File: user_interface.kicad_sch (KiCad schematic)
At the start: 14 parts, among them SW901 SW_SPDT

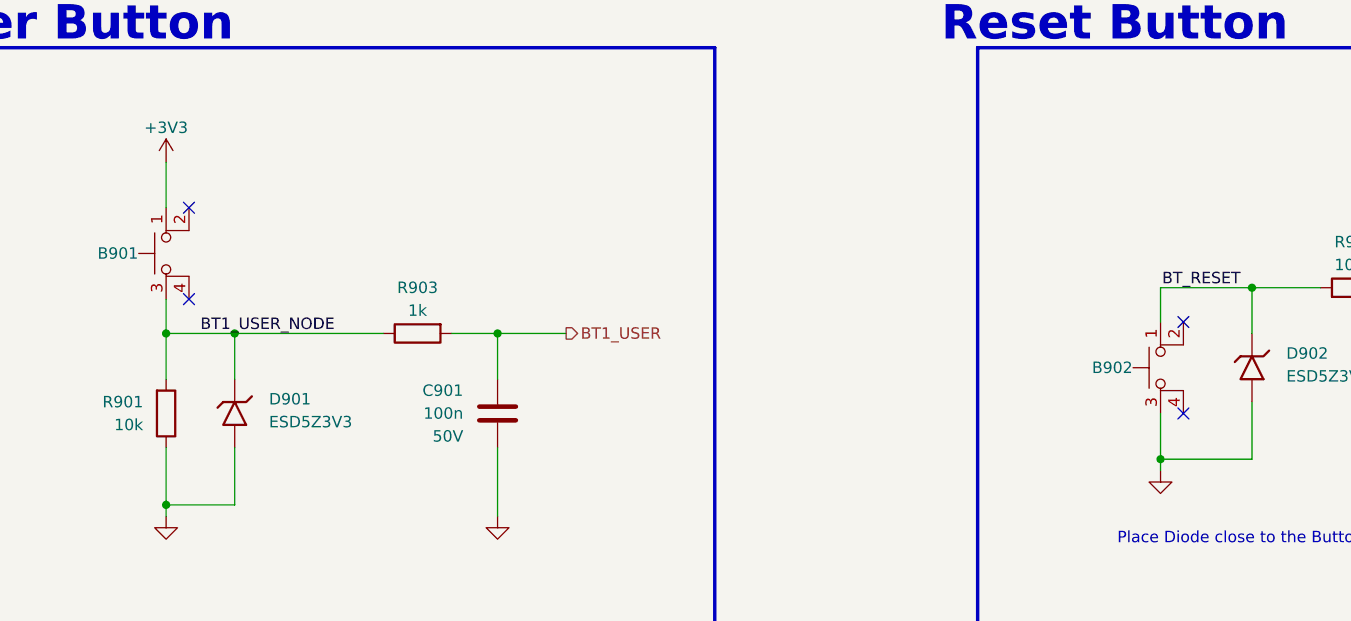
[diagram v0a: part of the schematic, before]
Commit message: Modified part number
Added 2nd Supplier
Added 2nd Mfr, Mfr NO.
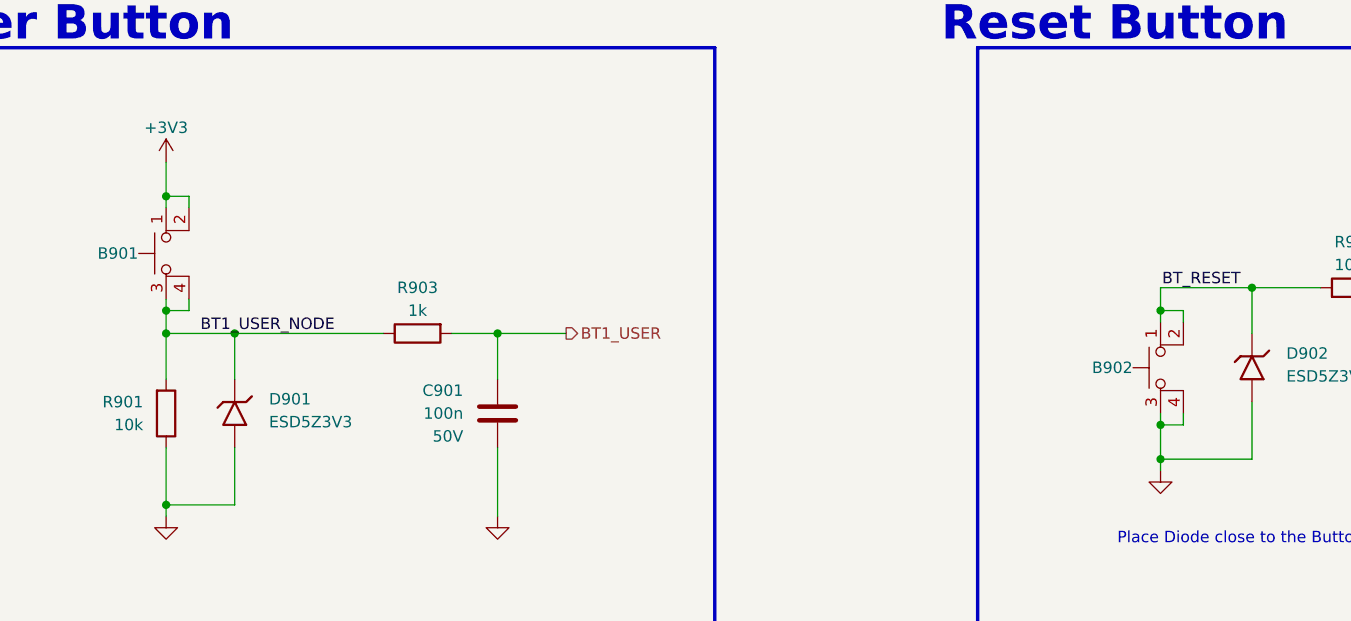
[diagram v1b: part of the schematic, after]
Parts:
- D901, D902, D903: now in the parts list
- R901, R904: Manufacturer 2nd (none) -> ROYALOHM; Manufacturer Part Number 2nd (none) -> 0402WGF1002TCE; Supplier 2nd (none) -> Electronisc Source; Supplier Part Number 2nd (none) -> 0150-3250-7
- R902: Manufacturer 2nd (none) -> ROYALOHM; Manufacturer Part Number 2nd (none) -> CQ02WGF1000TCE; Supplier 2nd (none) -> Electronisc Source; Supplier Part Number 2nd (none) -> 0150-4399-1
- R903, R905: Manufacturer 2nd (none) -> ROYALOHM; Manufacturer Part Number 2nd (none) -> 0402WGF1001TCE; Supplier 2nd (none) -> Electronisc Source; Supplier Part Number 2nd (none) -> 0150-3602-3
- SW901: Manufacturer DAWNING PRECISION -> (none); Manufacturer 2nd (none) -> DAWNING PRECISION; Manufacturer Part Number SS-B90AP-W-SP2-S085 -> (none); Manufacturer Part Number 2nd (none) -> SS-B90AP-W-SP2-S085; Supplier ES -> (none); Supplier 2nd (none) -> Electronisc Source; Supplier Part Number 1512-0003-4 -> (none); Supplier Part Number 2nd (none) -> 1512-0003-4; now in the parts list
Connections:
- net +3V3: now also B901.2
- net BT1_USER_NODE: now also B901.4
- net BT_RESET: now also B902.2
- net GND: now also B902.4
- no-connect marks 4 -> 0
